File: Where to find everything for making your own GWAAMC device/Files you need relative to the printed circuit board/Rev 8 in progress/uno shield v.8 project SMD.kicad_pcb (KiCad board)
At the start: 2 copper layers, 68.6 x 53.3 mm, 82 parts, among them J1 Conn_3.5mm, J2 Power, J3 Analog, J4 Digital, J5 Digital, J6 Conn_01x09_Female, J6_A7,A6 Conn_01x02_gender_unknown, J7_A7,A6 Conn_01x02_Female, J9 TE_1-2328702-0, P1 CONN_01X01, P2 CONN_01X01, P3 CONN_01X01, P4 CONN_01X01, Q1 MMBF5460 (2N5460), Q2 MMBF5460 (2N5460), Q3 DMN601K-7, Q4 DMN601K-7, Q5 DMN601K-7, Q6 DMN601K-7, Q7 DMN601K-7, U1 3V LDO, U2 AD8244ARMZ, U3 ADL5315ACPZ-R7, U4 REF200AU, U5 LM334M, U6 LM334M, U7 MCP4262-503E/UN, U8 - U32 all in parallel MCP4262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

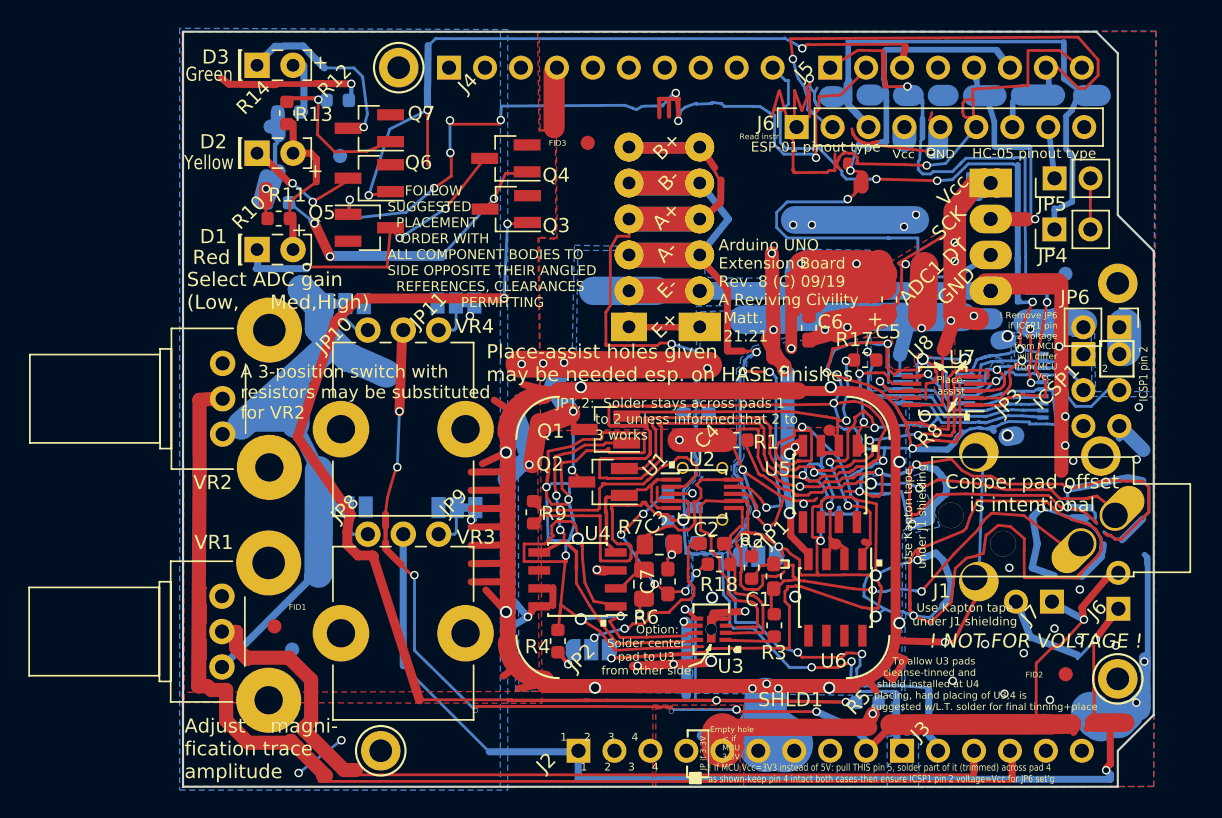
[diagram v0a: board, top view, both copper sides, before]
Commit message: Untested while I'm building it out
These KiCad and zipped gerber files are fully designed but not yet tested while I'm building the bare boards now.  I'm estimating mid- to late-October will see the final evaluation of operation of the entire device.
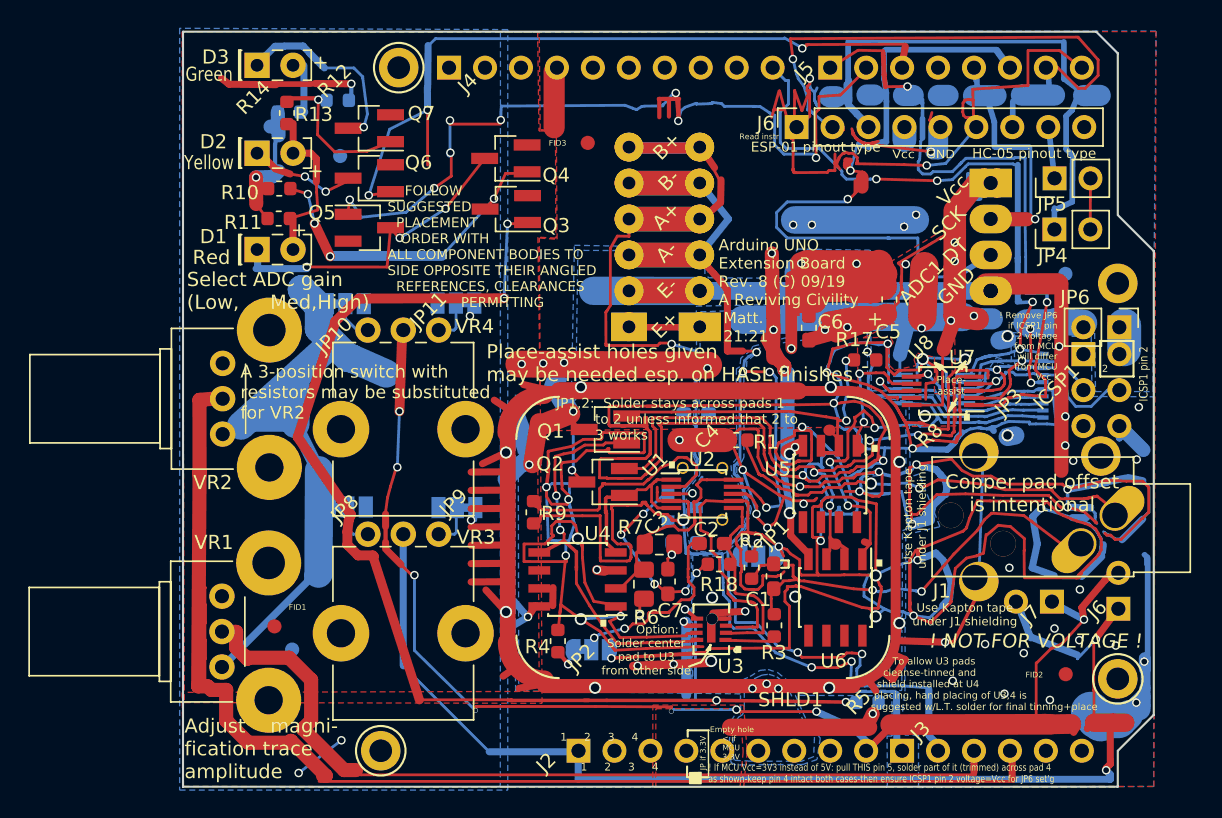
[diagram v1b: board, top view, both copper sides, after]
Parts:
- JP1, JP2: footprint Jumper:SolderJumper-3_P1.3mm_Open_RoundedPad1.0x1.5mm_NumberLabels -> Jumper:SolderJumper-3_P1.3mm_Bridged12_RoundedPad1.0x1.5mm_NumberLabels
- R10: moved to F.Cu
- moved R10 1.00 mm to (116.2, 90.6)
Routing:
- net GNDD: track 231.5 -> 223.7 mm
- net +5V: track 244.4 -> 240.1 mm
- net GNDA: track 198.2 -> 201.3 mm
- net Net-(Q3-Pad3): track 22.6 -> 23.7 mm, vias 3 -> 4
- net Net-(D2-Pad1): track 8.16 -> 7.36 mm
- net /6(**): track 62.0 -> 61.3 mm
- net Net-(D1-Pad2): track 11.8 -> 12.3 mm
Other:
- board text added: "3.3V operation will need this solder-jumpered (Pin 4) after scraping off solder mask, then modified per instructions."
- board text added: "C7"
- board text added: "GWAAM Sea Entanglement Gardening Aid"
- board text removed: "3.3V operation will need this solder-jumpered (Pin 4) and modified per instructions."
